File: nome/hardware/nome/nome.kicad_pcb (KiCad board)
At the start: 2 copper layers, 91.4 x 91.4 mm, 59 parts, among them J1 SJ-2524, J2 JTAG_SWD, J3 JST, J4 7SEG_DEBUG, SW1 SW_SPDT, SW2 Rotary_Encoder_Switch, U1 LM1117-1.8, U2 LM1117-3.3, U3 AS1115, U4 STMF411CEU6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

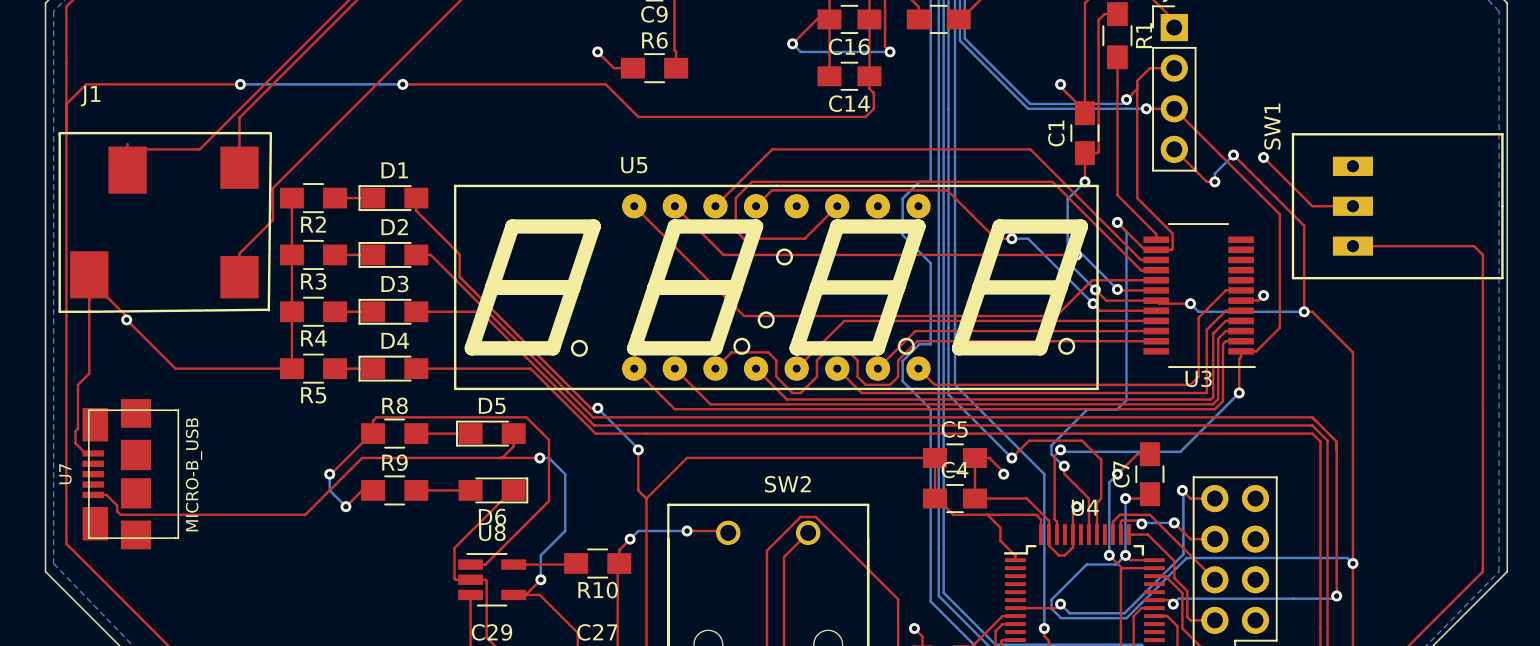
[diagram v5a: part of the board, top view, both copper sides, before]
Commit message: Correct USB direction and alignment
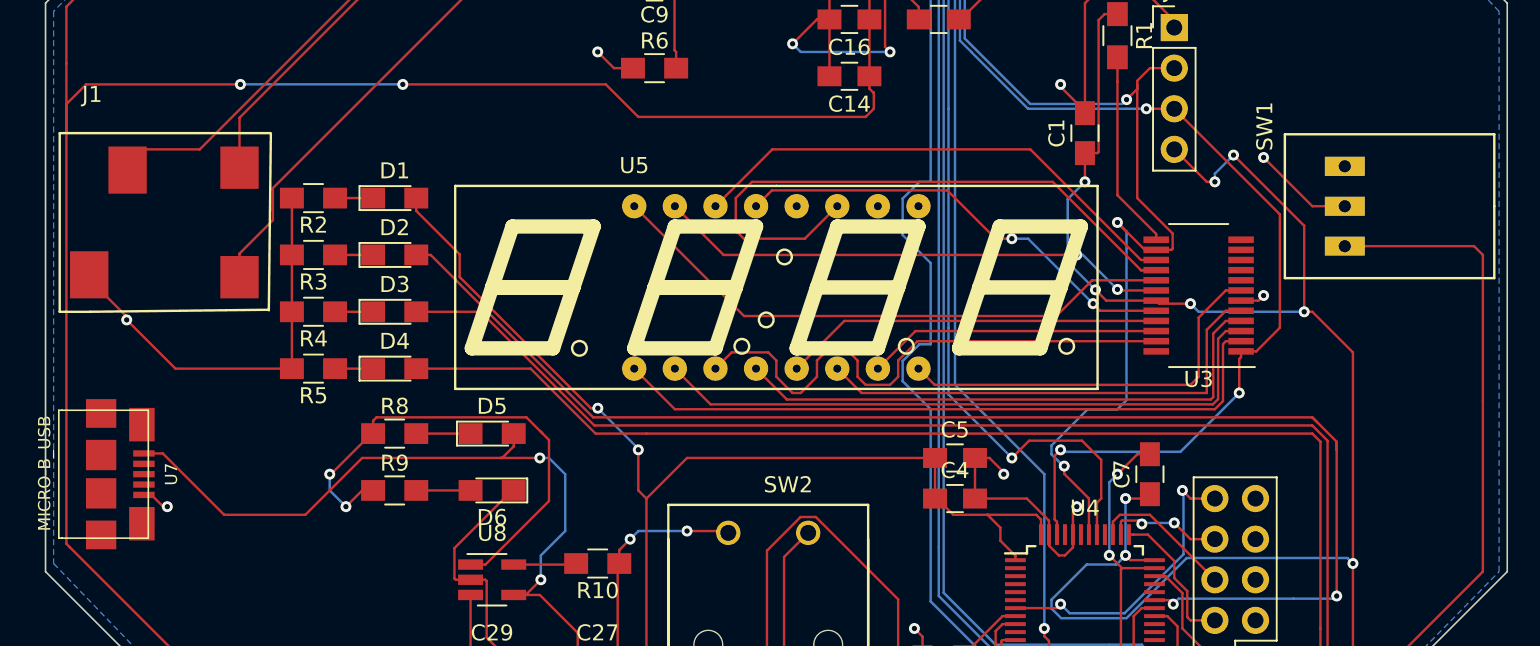
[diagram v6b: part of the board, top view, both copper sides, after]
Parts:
- moved U7 5.08 mm to (22.4, 95.5), turned to 270 degrees
- moved SW1 0.51 mm to (101.6, 78.7)
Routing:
- net GND: track 268.0 -> 255.9 mm, vias 23 -> 24
- net Net-(C27-Pad1): track 50.2 -> 47.9 mm
- net /HP_B: track 67.8 -> 66.2 mm
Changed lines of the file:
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@@
   (thickness 1.6)
   (drawings 8)
-  (tracks 922)
+  (tracks 915)
   (zones 0)
   (modules 59)
@@
   )
   (module nome:CK_SPDT (layer F.Cu)
-    (at 102.108 78.74 90)
+    (at 101.6 78.74 90)
     (fp_text reference SW1 (at 5 -5 90) (layer F.SilkS)
       (effects (font (size 1 1) (thickness 0.15)))
@@
   )
   (module open-project:MICRO-B_USB (layer F.Cu)
-    (at 27.432 95.504 90)
-    (fp_text reference U7 (at 0 -5.842 90) (layer F.SilkS)
+    (at 22.352 95.504 270)
+    (fp_text reference U7 (at 0 -5.842 270) (layer F.SilkS)
       (effects (font (size 0.762 0.762) (thickness 0.127)))
     )
-    (fp_text value MICRO-B_USB (at -0.05 2.09 90) (layer F.SilkS)
+    (fp_text value MICRO-B_USB (at -0.05 2.09 270) (layer F.SilkS)
       (effects (font (size 0.762 0.762) (thickness 0.127)))
     )
@@
     (fp_line (start 4.0005 1.19888) (end -4.0005 1.19888) (layer F.SilkS) (width 0.09906))
     (fp_line (start -4.0005 1.00076) (end -4.0005 -4.39928) (layer F.SilkS) (width 0.09906))
-    (pad "" smd rect (at -1.19888 -1.4478 90) (size 1.89738 1.89738) (layers F.Cu F.Paste F.Mask))
-    (pad "" smd rect (at 1.19888 -1.4478 90) (size 1.89992 1.89738) (layers F.Cu F.Paste F.Mask))
-    (pad "" smd rect (at 3.79984 -1.4478 90) (size 1.79578 1.89738) (layers F.Cu F.Paste F.Mask))
-    (pad "" smd rect (at -3.0988 -3.99796 90) (size 2.0955 1.59766) (layers F.Cu F.Paste F.Mask))
-    (pad 1 smd rect (at -1.29794 -4.12496 90) (size 0.39878 1.3462) (layers F.Cu F.Paste F.Mask)
+    (pad "" smd rect (at -1.19888 -1.4478 270) (size 1.89738 1.89738) (layers F.Cu F.Paste F.Mask))
+    (pad "" smd rect (at 1.19888 -1.4478 270) (size 1.89992 1.89738) (layers F.Cu F.Paste F.Mask))
+    (pad "" smd rect (at 3.79984 -1.4478 270) (size 1.79578 1.89738) (layers F.Cu F.Paste F.Mask))
+    (pad "" smd rect (at -3.0988 -3.99796 270) (size 2.0955 1.59766) (layers F.Cu F.Paste F.Mask))
+    (pad 1 smd rect (at -1.29794 -4.12496 270) (size 0.39878 1.3462) (layers F.Cu F.Paste F.Mask)
       (net 15 "Net-(C27-Pad1)") (clearance 0.2032))
-    (pad 2 smd rect (at -0.6477 -4.12496 90) (size 0.39878 1.3462) (layers F.Cu F.Paste F.Mask)
+    (pad 2 smd rect (at -0.6477 -4.12496 270) (size 0.39878 1.3462) (layers F.Cu F.Paste F.Mask)
       (net 103 "Net-(U7-Pad2)") (clearance 0.2032))
-    (pad 3 smd rect (at 0 -4.12496 90) (size 0.39878 1.3462) (layers F.Cu F.Paste F.Mask)
+    (pad 3 smd rect (at 0 -4.12496 270) (size 0.39878 1.3462) (layers F.Cu F.Paste F.Mask)
       (net 104 "Net-(U7-Pad3)") (clearance 0.2032))
-    (pad 4 smd rect (at 0.6477 -4.12496 90) (size 0.39878 1.3462) (layers F.Cu F.Paste F.Mask)
+    (pad 4 smd rect (at 0.6477 -4.12496 270) (size 0.39878 1.3462) (layers F.Cu F.Paste F.Mask)
       (net 105 "Net-(U7-Pad4)") (clearance 0.2032))
-    (pad 5 smd rect (at 1.29794 -4.12496 90) (size 0.39878 1.3462) (layers F.Cu F.Paste F.Mask)
+    (pad 5 smd rect (at 1.29794 -4.12496 270) (size 0.39878 1.3462) (layers F.Cu F.Paste F.Mask)
       (net 106 GND) (clearance 0.2032))
-    (pad "" smd rect (at 3.0988 -3.99796 90) (size 2.0955 1.59766) (layers F.Cu F.Paste F.Mask))
-    (pad "" smd rect (at -3.79984 -1.4478 90) (size 1.79578 1.89738) (layers F.Cu F.Paste F.Mask))
+    (pad "" smd rect (at 3.0988 -3.99796 270) (size 2.0955 1.59766) (layers F.Cu F.Paste F.Mask))
+    (pad "" smd rect (at -3.79984 -1.4478 270) (size 1.79578 1.89738) (layers F.Cu F.Paste F.Mask))
   )
   (module Capacitors_SMD:C_0805_HandSoldering (layer F.Cu)
@@
   (segment (start 74.676 46.736) (end 73.152 46.736) (width 0.1524) (layer F.Cu) (net 2))
   (segment (start 75.184 47.244) (end 74.676 46.736) (width 0.1524) (layer F.Cu) (net 2))
+  (segment (start 48.768 94.488) (end 40.132 94.488) (width 0.1524) (layer F.Cu) (net 15))
+  (segment (start 40.132 94.488) (end 36.576 98.044) (width 0.1524) (layer F.Cu) (net 15))
+  (segment (start 36.576 98.044) (end 31.496 98.044) (width 0.1524) (layer F.Cu) (net 15))
+  (segment (start 31.496 98.044) (end 27.65806 94.20606) (width 0.1524) (layer F.Cu) (net 15))
+  (segment (start 27.65806 94.20606) (end 26.47696 94.20606) (width 0.1524) (layer F.Cu) (net 15))
+  (segment (start 26.47696 96.80194) (end 26.95067 96.80194) (width 0.1524) (layer F.Cu) (net 106))
+  (segment (start 26.95067 96.80194) (end 27.68473 97.536) (width 0.1524) (layer F.Cu) (net 106))
+  (segment (start 27.68473 97.536) (end 27.94 97.536) (width 0.1524) (layer F.Cu) (net 106))
+  (via (at 27.94 97.536) (size 0.6858) (drill 0.3302) (layers F.Cu B.Cu) (net 106))
   (segment (start 79.482 48.26) (end 79.357 48.26) (width 0.1524) (layer F.Cu) (net 106))
   (segment (start 71.862 63.5) (end 71.737 63.5) (width 0.1524) (layer F.Cu) (net 2))
@@
   (segment (start 54.364 56.388) (end 62.992 56.388) (width 0.1524) (layer F.Cu) (net 5))
   (segment (start 51.872 51.308) (end 51.872 47.534) (width 0.1524) (layer F.Cu) (net 5))
-  (segment (start 25.456 74.8536) (end 25.456 76.481) (width 0.1524) (layer F.Cu) (net 5))
   (segment (start 70.9495 58.42) (end 68.9175 56.388) (width 0.1524) (layer B.Cu) (net 5))
   (segment (start 68.9175 56.388) (end 62.992 56.388) (width 0.1524) (layer B.Cu) (net 5))
@@
   (segment (start 51.2445 94.488) (end 51.816 94.488) (width 0.1524) (layer B.Cu) (net 15))
   (segment (start 48.768 94.488) (end 48.8884 94.488) (width 0.1524) (layer F.Cu) (net 15))
-  (segment (start 40.132 94.488) (end 48.768 94.488) (width 0.1524) (layer F.Cu) (net 15))
   (segment (start 48.768 94.488) (end 51.2445 94.488) (width 0.1524) (layer F.Cu) (net 15))
   (via (at 51.2445 94.488) (size 0.6858) (drill 0.3302) (layers F.Cu B.Cu) (net 15))
-  (segment (start 23.30704 96.80194) (end 24.13254 96.80194) (width 0.1524) (layer F.Cu) (net 15))
-  (segment (start 24.13254 96.80194) (end 24.806909 97.476309) (width 0.1524) (layer F.Cu) (net 15))
-  (segment (start 36.576 98.044) (end 40.132 94.488) (width 0.1524) (layer F.Cu) (net 15))
-  (segment (start 24.806909 97.476309) (end 24.806909 97.834451) (width 0.1524) (layer F.Cu) (net 15))
-  (segment (start 24.806909 97.834451) (end 25.016458 98.044) (width 0.1524) (layer F.Cu) (net 15))
   (segment (start 48.8884 94.488) (end 49.61 93.7664) (width 0.1524) (layer F.Cu) (net 15))
-  (segment (start 25.016458 98.044) (end 36.576 98.044) (width 0.1524) (layer F.Cu) (net 15))
   (segment (start 49.61 93.7664) (end 49.61 92.964) (width 0.1524) (layer F.Cu) (net 15))
   (segment (start 57.81 123.5984) (end 57.81 122.696) (width 0.1524) (layer F.Cu) (net 16))
@@
   (segment (start 25.4 85.65) (end 25.4 85.852) (width 0.1524) (layer F.Cu) (net 106))
   (via (at 25.4 85.852) (size 0.6858) (drill 0.3302) (layers F.Cu B.Cu) (net 106))
-  (segment (start 23.30704 94.20606) (end 22.83333 94.20606) (width 0.1524) (layer F.Cu) (net 106))
-  (segment (start 22.83333 94.20606) (end 22.198899 93.571629) (width 0.1524) (layer F.Cu) (net 106))
-  (segment (start 22.198899 93.571629) (end 22.198899 92.810899) (width 0.1524) (layer F.Cu) (net 106))
-  (segment (start 22.198899 92.810899) (end 22.352 92.657798) (width 0.1524) (layer F.Cu) (net 106))
-  (segment (start 22.352 92.657798) (end 22.352 89.916) (width 0.1524) (layer F.Cu) (net 106))
-  (segment (start 22.352 89.916) (end 23.056 89.212) (width 0.1524) (layer F.Cu) (net 106))
-  (segment (start 23.056 89.212) (end 23.056 83.031) (width 0.1524) (layer F.Cu) (net 106))
   (segment (start 63.5 60.686) (end 63.5 62.484) (width 0.1524) (layer F.Cu) (net 106))
   (segment (start 63.5 62.484) (end 62.992 62.992) (width 0.1524) (layer F.Cu) (net 106))
@@
   (via (at 96.52 75.692) (size 0.6858) (drill 0.3302) (layers F.Cu B.Cu) (net 106))
   (segment (start 67.97 118.096) (end 67.72 118.096) (width 0.1524) (layer F.Cu) (net 106))
-  (segment (start 23.056 83.031) (end 23.056 84.6584) (width 0.1524) (layer F.Cu) (net 106))
   (segment (start 78.466 97.028) (end 81.711066 97.028) (width 0.1524) (layer F.Cu) (net 106))
   (segment (start 81.711066 97.028) (end 83.094 98.410934) (width 0.1524) (layer F.Cu) (net 106))

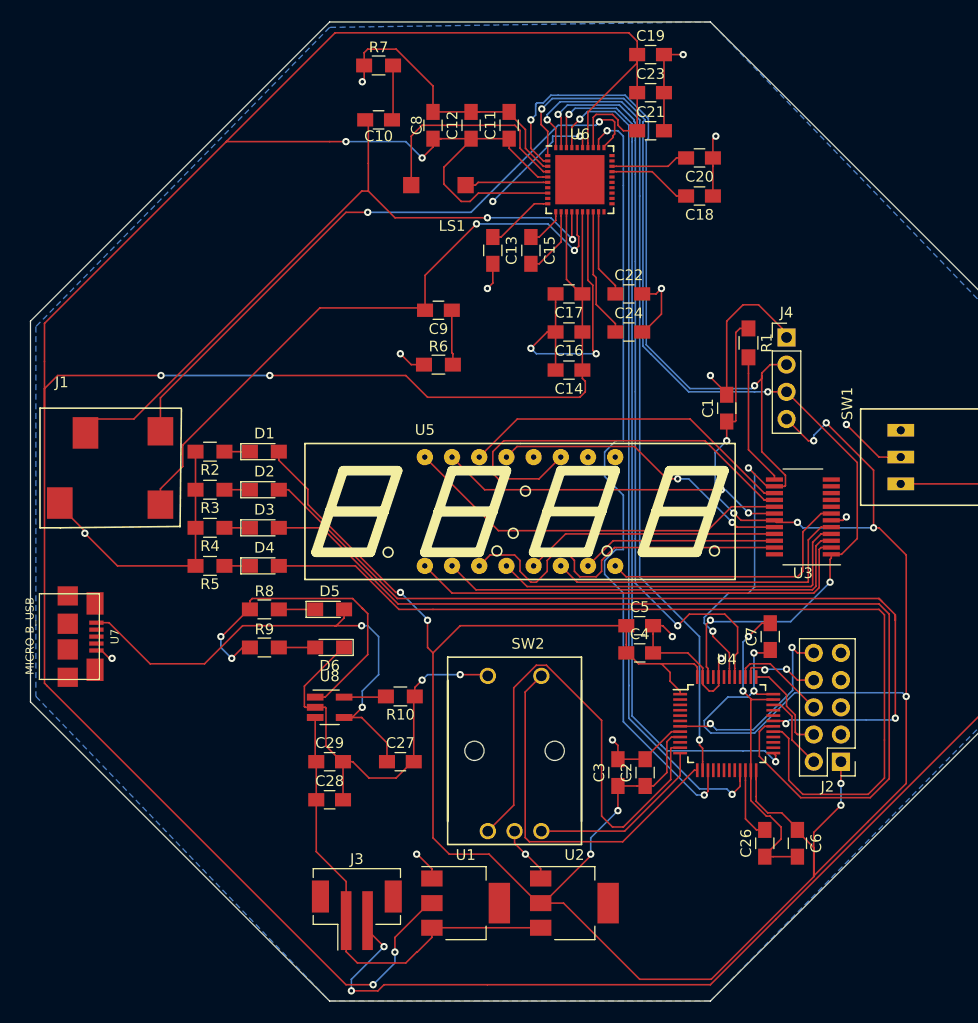
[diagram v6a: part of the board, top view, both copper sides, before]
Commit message: Move power rail sizes to 12mil
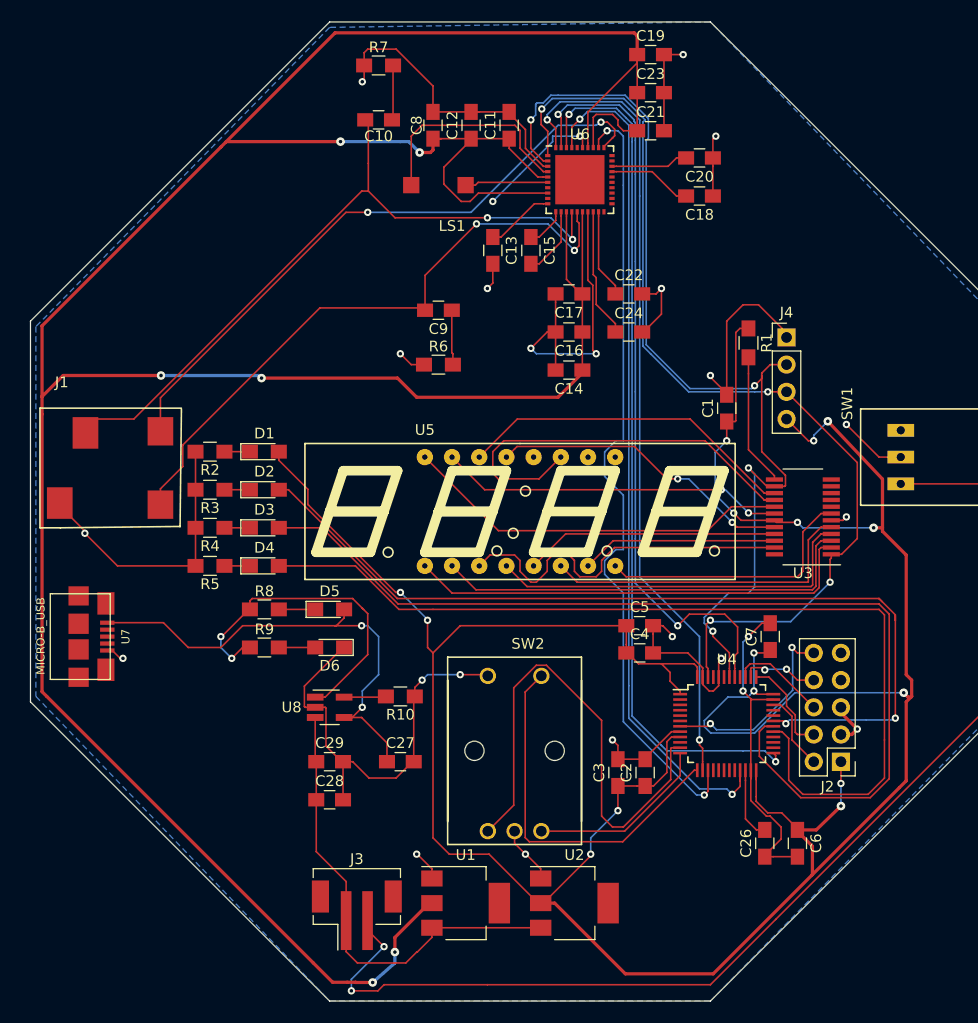
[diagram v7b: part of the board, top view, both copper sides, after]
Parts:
- moved U7 1.02 mm to (23.4, 95.5)
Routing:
- net GND: track 255.9 -> 260.3 mm, vias 24 -> 25
- net Net-(C27-Pad1): track 47.9 -> 45.6 mm
- net +1V8: track 309.7 -> 307.8 mm
- net +3V3: track 292.5 -> 290.9 mm
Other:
- net class 1.8V added: clearance 0.1524, trace_width 0.305, via_dia 0.8, via_drill 0.3302
- net class 3.3V added: clearance 0.1524, trace_width 0.305, via_dia 0.8, via_drill 0.3302
